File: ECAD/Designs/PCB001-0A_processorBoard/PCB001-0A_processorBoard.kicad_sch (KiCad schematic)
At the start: 0 parts

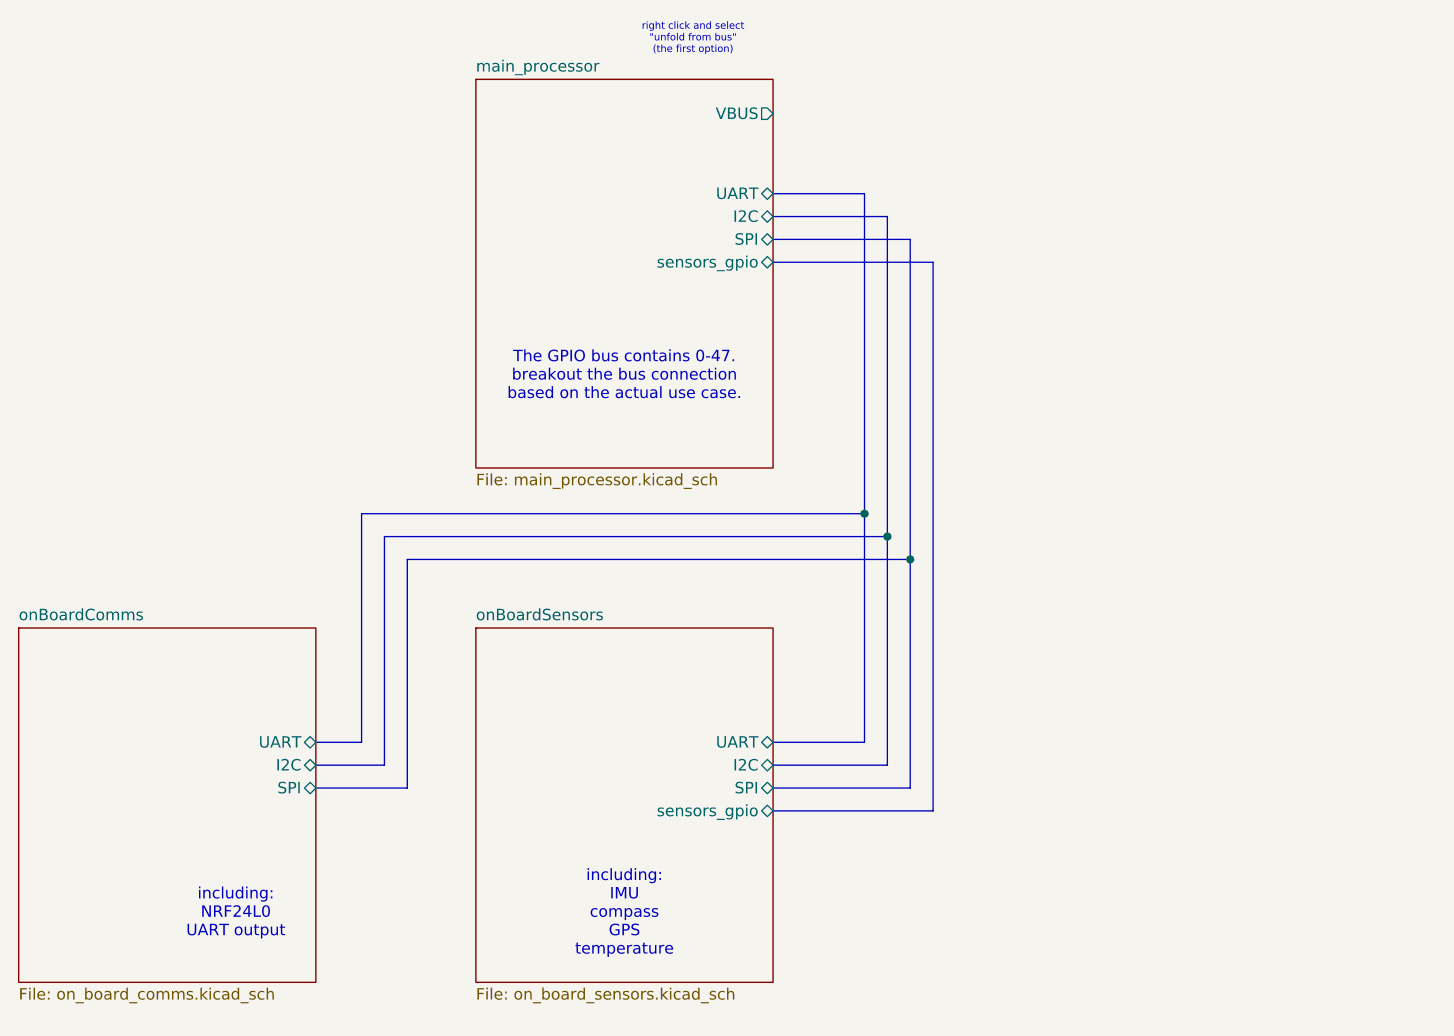
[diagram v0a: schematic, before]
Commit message: added off board sensors page, included more gpio (see google drive), and tracked the gpio better
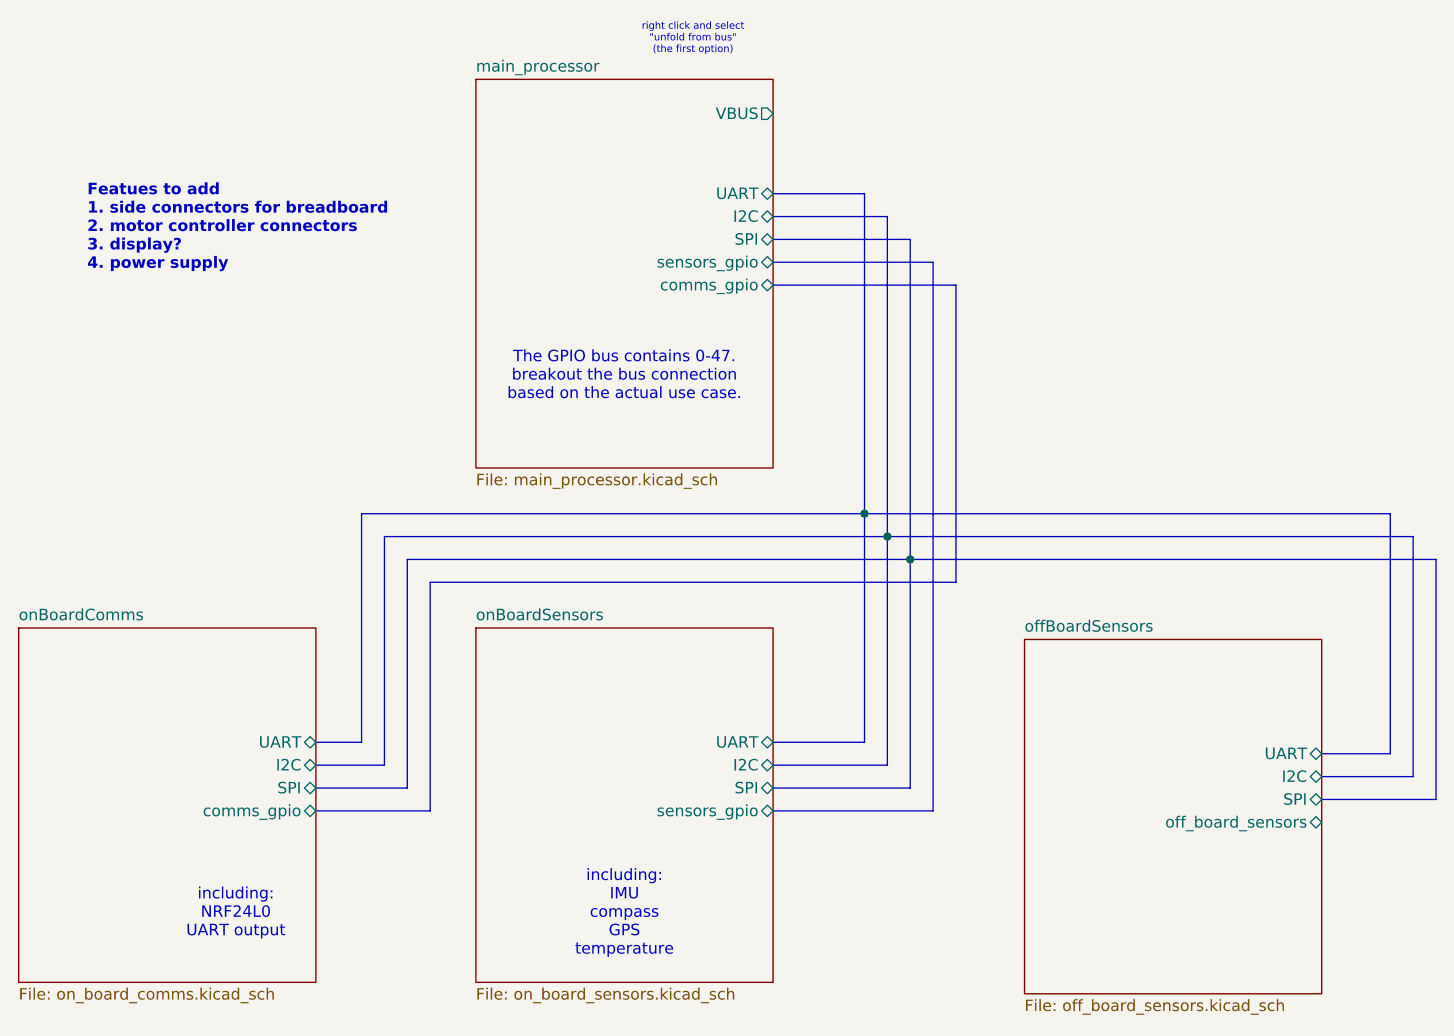
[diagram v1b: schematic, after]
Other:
- added sheet offBoardSensors (off_board_sensors.kicad_sch)
- sheet main_processor ports: added comms_gpio; removed none
- sheet onBoardComms ports: added comms_gpio; removed none
- note added: "Featues to add 1. side connectors for breadboard 2. motor controller connectors 3. display? 4. power supply"
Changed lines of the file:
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@@
+		)
+	)
+	(text "Featues to add\n1. side connectors for breadboard\n2. motor controller connectors\n3. display?\n4. power supply"
+		(exclude_from_sim no)
+		(at 83.82 69.85 0)
+		(effects
+			(font
+				(size 1.27 1.27)
+				(thickness 0.254)
+				(bold yes)
+			)
+			(justify left)
 		)
 	)
@@
 	(bus
 		(pts
+			(xy 233.68 106.68) (xy 233.68 133.35)
+		)
+		(stroke
+			(width 0)
+			(type default)
+		)
+	)
+	(bus
+		(pts
+			(xy 220.98 133.35) (xy 233.68 133.35)
+		)
+		(stroke
+			(width 0)
+			(type default)
+		)
+	)
+	(bus
+		(pts
 			(xy 160.02 129.54) (xy 172.72 129.54)
 		)
@@
 	(bus
 		(pts
+			(xy 220.98 130.81) (xy 231.14 130.81)
+		)
+		(stroke
+			(width 0)
+			(type default)
+		)
+	)
+	(bus
+		(pts
 			(xy 160.02 68.58) (xy 172.72 68.58)
 		)
@@
 	(bus
 		(pts
+			(xy 220.98 128.27) (xy 228.6 128.27)
+		)
+		(stroke
+			(width 0)
+			(type default)
+		)
+	)
+	(bus
+		(pts
 			(xy 160.02 73.66) (xy 177.8 73.66)
 		)
@@
 	(bus
 		(pts
+			(xy 180.34 76.2) (xy 180.34 109.22)
+		)
+		(stroke
+			(width 0)
+			(type default)
+		)
+	)
+	(bus
+		(pts
+			(xy 175.26 106.68) (xy 233.68 106.68)
+		)
+		(stroke
+			(width 0)
+			(type default)
+		)
+	)
+	(bus
+		(pts
+			(xy 228.6 101.6) (xy 228.6 128.27)
+		)
+		(stroke
+			(width 0)
+			(type default)
+		)
+	)
+	(bus
+		(pts
+			(xy 121.92 109.22) (xy 180.34 109.22)
+		)
+		(stroke
+			(width 0)
+			(type default)
+		)
+	)
+	(bus
+		(pts
+			(xy 121.92 109.22) (xy 121.92 134.62)
+		)
+		(stroke
+			(width 0)
+			(type default)
+		)
+	)
+	(bus
+		(pts
+			(xy 160.02 76.2) (xy 180.34 76.2)
+		)
+		(stroke
+			(width 0)
+			(type default)
+		)
+	)
+	(bus
+		(pts
 			(xy 160.02 71.12) (xy 175.26 71.12)
 		)
@@
 	(bus
 		(pts
+			(xy 170.18 101.6) (xy 228.6 101.6)
+		)
+		(stroke
+			(width 0)
+			(type default)
+		)
+	)
+	(bus
+		(pts
 			(xy 114.3 101.6) (xy 170.18 101.6)
 		)
@@
 		(pts
 			(xy 109.22 132.08) (xy 119.38 132.08)
+		)
+		(stroke
+			(width 0)
+			(type default)
+		)
+	)
+	(bus
+		(pts
+			(xy 109.22 134.62) (xy 121.92 134.62)
+		)
+		(stroke
+			(width 0)
+			(type default)
+		)
+	)
+	(bus
+		(pts
+			(xy 231.14 104.14) (xy 231.14 130.81)
+		)
+		(stroke
+			(width 0)
+			(type default)
+		)
+	)
+	(bus
+		(pts
+			(xy 172.72 104.14) (xy 231.14 104.14)
 		)
 		(stroke
@@
 			)
 		)
+		(pin "comms_gpio" bidirectional
+			(at 160.02 76.2 0)
+			(effects
+				(font
+					(size 1.27 1.27)
+				)
+				(justify right)
+			)
+		)
 		(instances
 			(project "PCB001-0A_processorBoard"
@@
 			)
 		)
+		(pin "comms_gpio" bidirectional
+			(at 109.22 134.62 0)
+			(effects
+				(font
+					(size 1.27 1.27)
+				)
+				(justify right)
+			)
+		)
 		(instances
 			(project "PCB001-0A_processorBoard"
@@
 				)
 			)
+		)
+	)
+	(sheet
+		(at 187.96 115.57)
+		(size 33.02 39.37)
+		(exclude_from_sim no)
+		(in_bom yes)
+		(on_board yes)
+		(dnp no)
+		(fields_autoplaced yes)
+		(stroke
+			(width 0.1524)
+			(type solid)
+			(color 72 0 72 1)
+		)
+		(fill
+			(color 255 255 194 1.0000)
+		)
+		(property "Sheetname" "offBoardSensors"
+			(at 187.96 114.8584 0)
+			(effects
+				(font
+					(size 1.27 1.27)
+				)
+				(justify left bottom)
+			)
+		)
+		(property "Sheetfile" "off_board_sensors.kicad_sch"
+			(at 187.96 155.5246 0)
+			(effects
+				(font
+					(size 1.27 1.27)
+				)
+				(justify left top)
+			)
+		)
+		(pin "I2C" bidirectional
+			(at 220.98 130.81 0)
+			(effects
+				(font
+					(size 1.27 1.27)
+				)
+				(justify right)
+			)
+		)
+		(pin "SPI" bidirectional
+			(at 220.98 133.35 0)
+			(effects
+				(font
+					(size 1.27 1.27)
+				)
+				(justify right)
+			)
+		)
+		(pin "UART" bidirectional
+			(at 220.98 128.27 0)
+			(effects
+				(font
+					(size 1.27 1.27)
+				)
+				(justify right)
+			)
+		)
+		(pin "off_board_sensors" bidirectional
+			(at 220.98 135.89 0)
+			(effects
+				(font
+					(size 1.27 1.27)
+				)
+				(justify right)
+			)
+		)
+		(instances
+			(project "PCB001-0A_processorBoard"
+				(path "/c85d256f-82d8-4180-ad51-faa565e237b8"
+					(page "6")
+				)
+			)
